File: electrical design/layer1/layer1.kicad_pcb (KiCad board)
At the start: 2 copper layers, 178 x 168.1 mm, 211 parts, among them J1 XT60-F, J2 1x07 2.54 FEMALE, J3 1x07 2.54 FEMALE, J4 XT30PW-F, J5 Conn_01x01_Socket, J6 Conn_01x01_Socket, J7 Conn_01x01_Socket, J8 Conn_01x01_Socket, Q1 MOSFET-NCH-FQP30N06L, Q2 MOSFET-NCH-AO3404A, SW1 SW_DPDT_x2, U1 CD74HC4067SM, U2 CD74HC4067SM

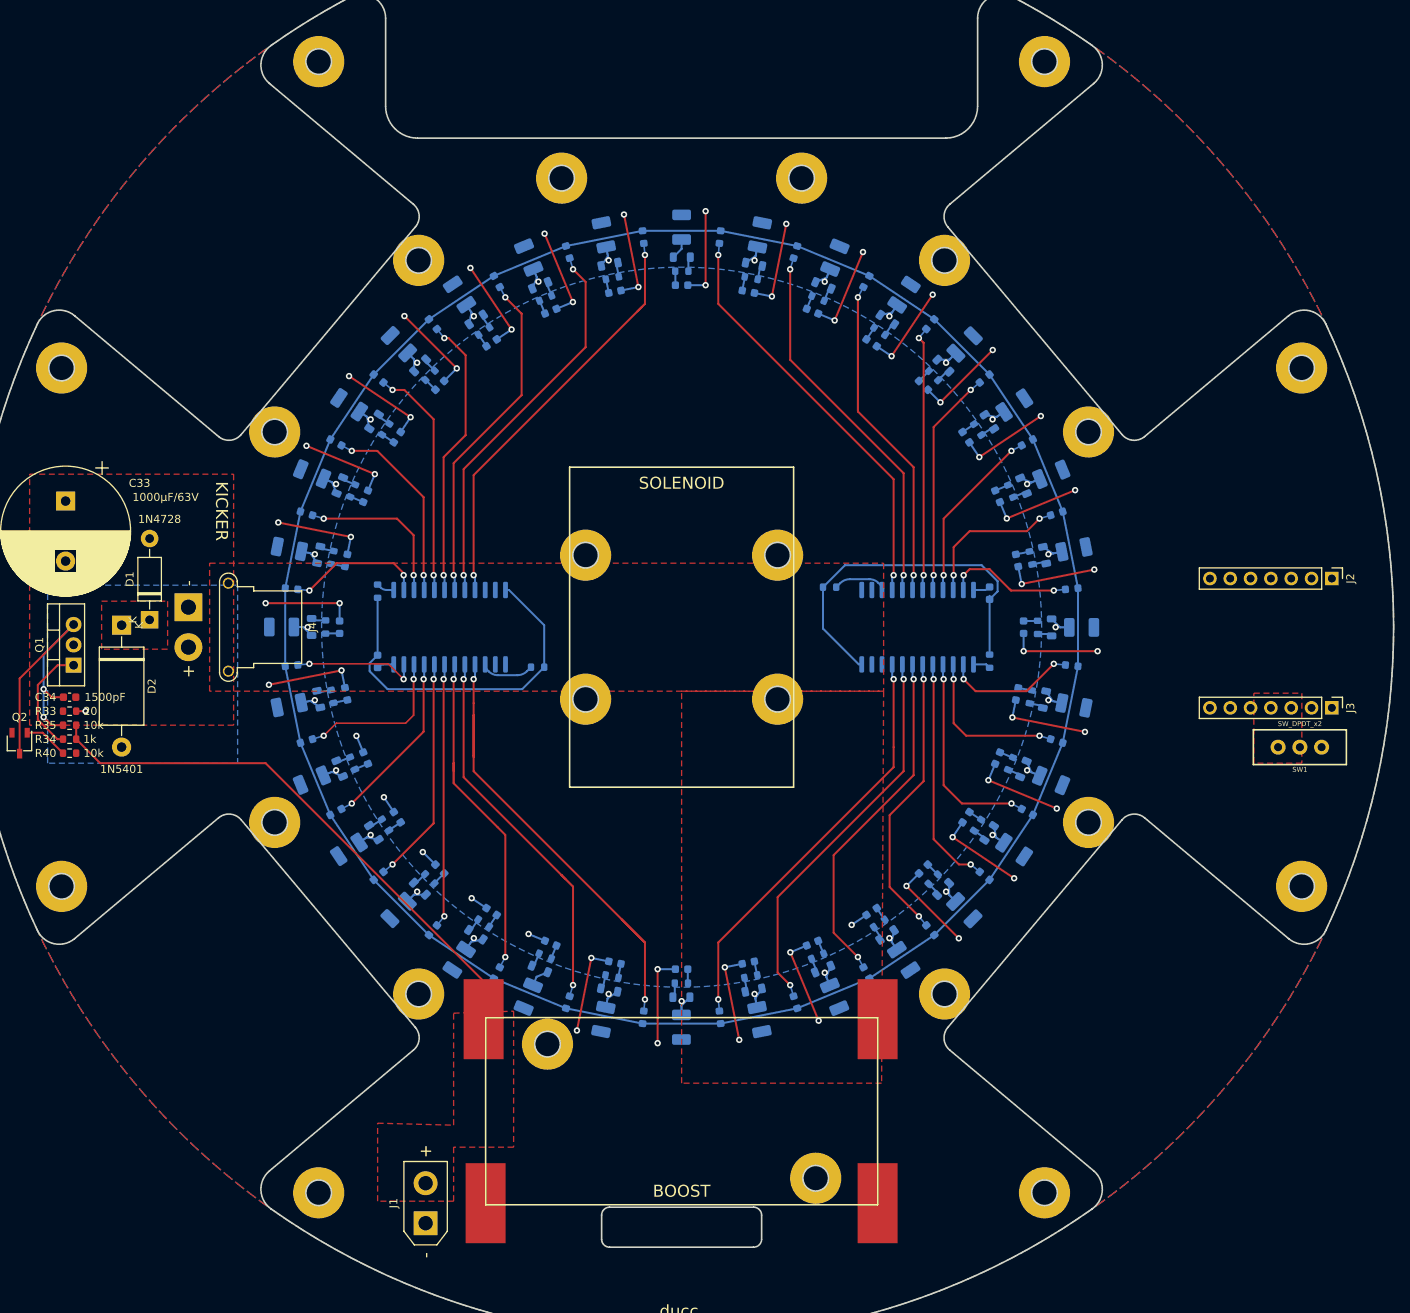
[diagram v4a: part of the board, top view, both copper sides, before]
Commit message: route l1 signal lines and resolve drc issues
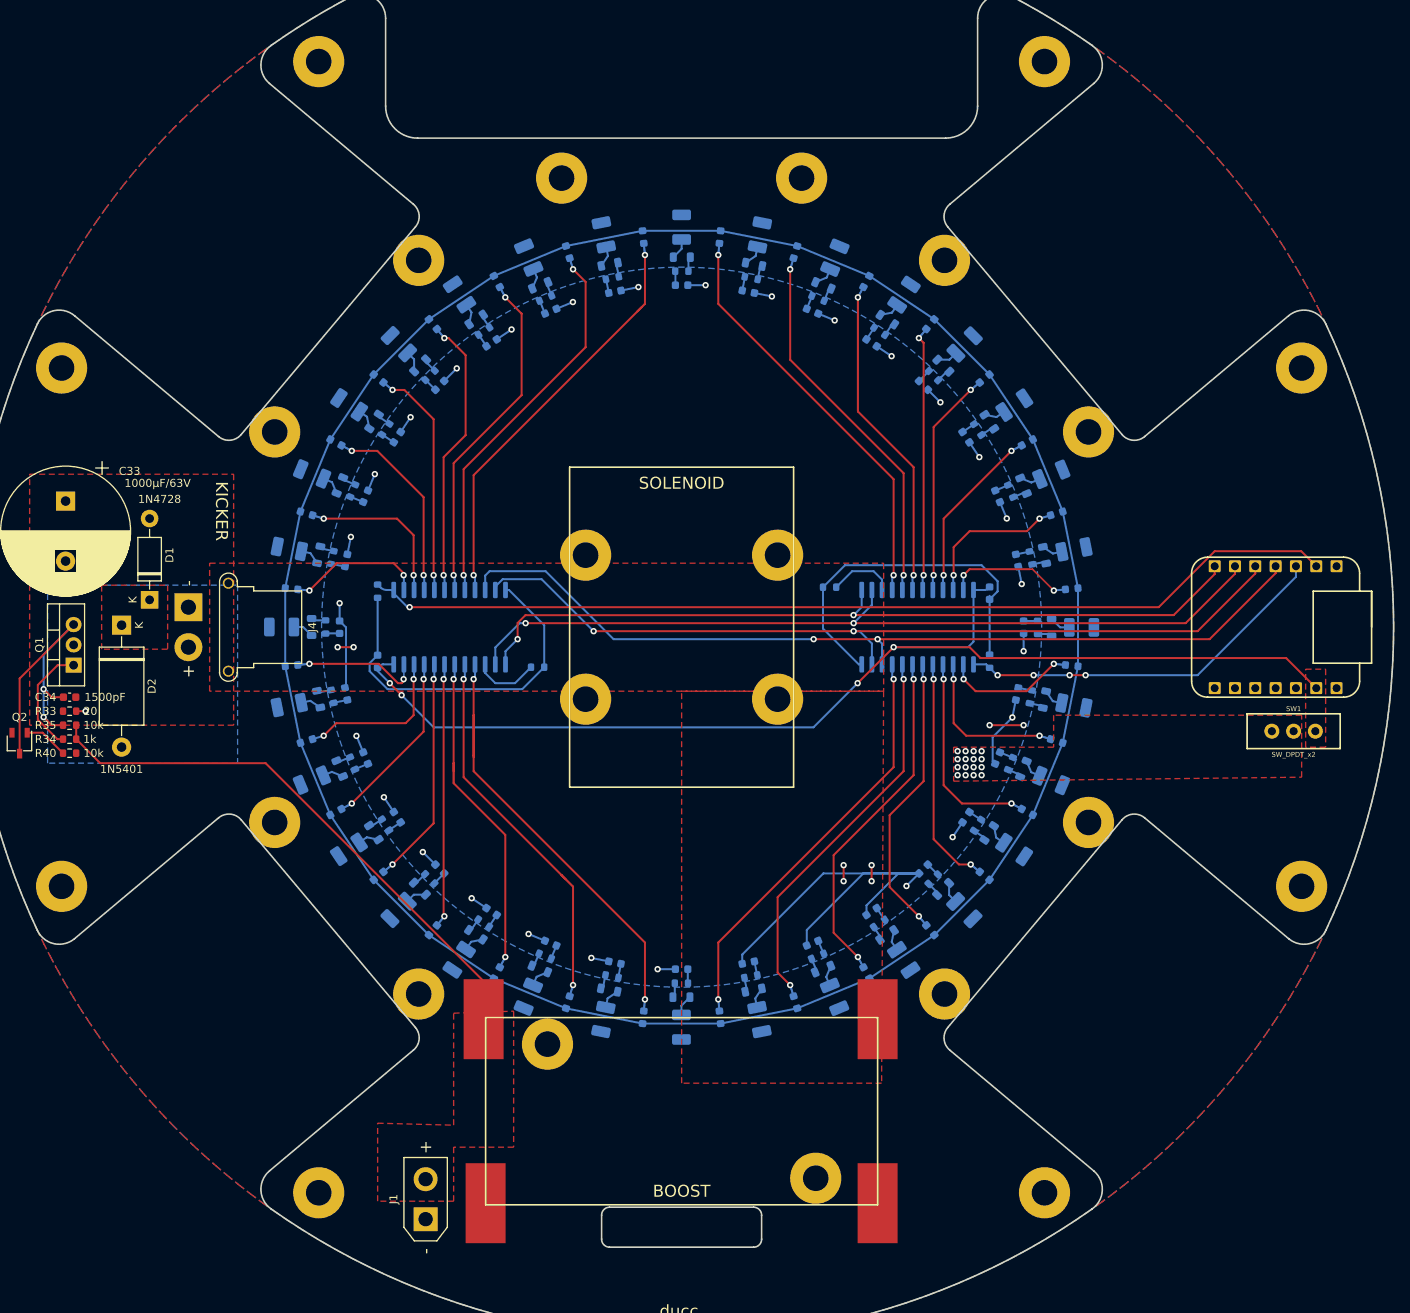
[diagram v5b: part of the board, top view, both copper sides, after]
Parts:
- removed J2, J3: 1x07 2.54 FEMALE, Connector_PinHeader_2.54mm:PinHeader_1x07_P2.54mm_Vertical
- added U3: MOUDLE-SEEEDUINO-XIAO-ESP32C3, libraries:xiao-esp32c3, F.Cu at (179.2, 105.0)
- moved D1 2.50 mm to (38.5, 101.6)
- moved SW1 2.15 mm to (181.5, 118.0), turned to -90 degrees
- moved J1 0.50 mm to (73.0, 179.0)
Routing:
- net GND: track 311.7 -> 131.6 mm, vias 58 -> 27
- net +3V3: track 4.59 -> 148.1 mm, vias 0 -> 4
- net /MUX1OUT: track 2.47 -> 122.6 mm, vias 0 -> 1
- net /S0: track 0.00 -> 112.0 mm, vias 0 -> 2
- net /S1: track 0.00 -> 107.9 mm, vias 0 -> 2
- net /S2: track 0.00 -> 104.4 mm, vias 0 -> 2
- net /S3: track 0.00 -> 100.0 mm, vias 0 -> 2
- net /MUX2OUT: track 2.19 -> 47.3 mm, vias 0 -> 4
- net Net-(SW1A-B): track 56.3 -> 66.6 mm, vias 0 -> 24
- net Net-(U1-I15): track 61.7 -> 59.0 mm
- net Net-(U1-I8): track 15.9 -> 17.9 mm
- net Net-(U2-~{E}): track 6.77 -> 8.29 mm
- net Net-(LED5-A): track 4.12 -> 2.65 mm, vias 1 -> 0
- net Net-(LED21-A): track 4.12 -> 2.65 mm, vias 1 -> 0
- net Net-(LED29-A): track 4.12 -> 2.65 mm, vias 1 -> 0
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- added copper zone on F.Cu, net Net-(SW1A-B)
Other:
- outline, holes or cut-outs redrawn

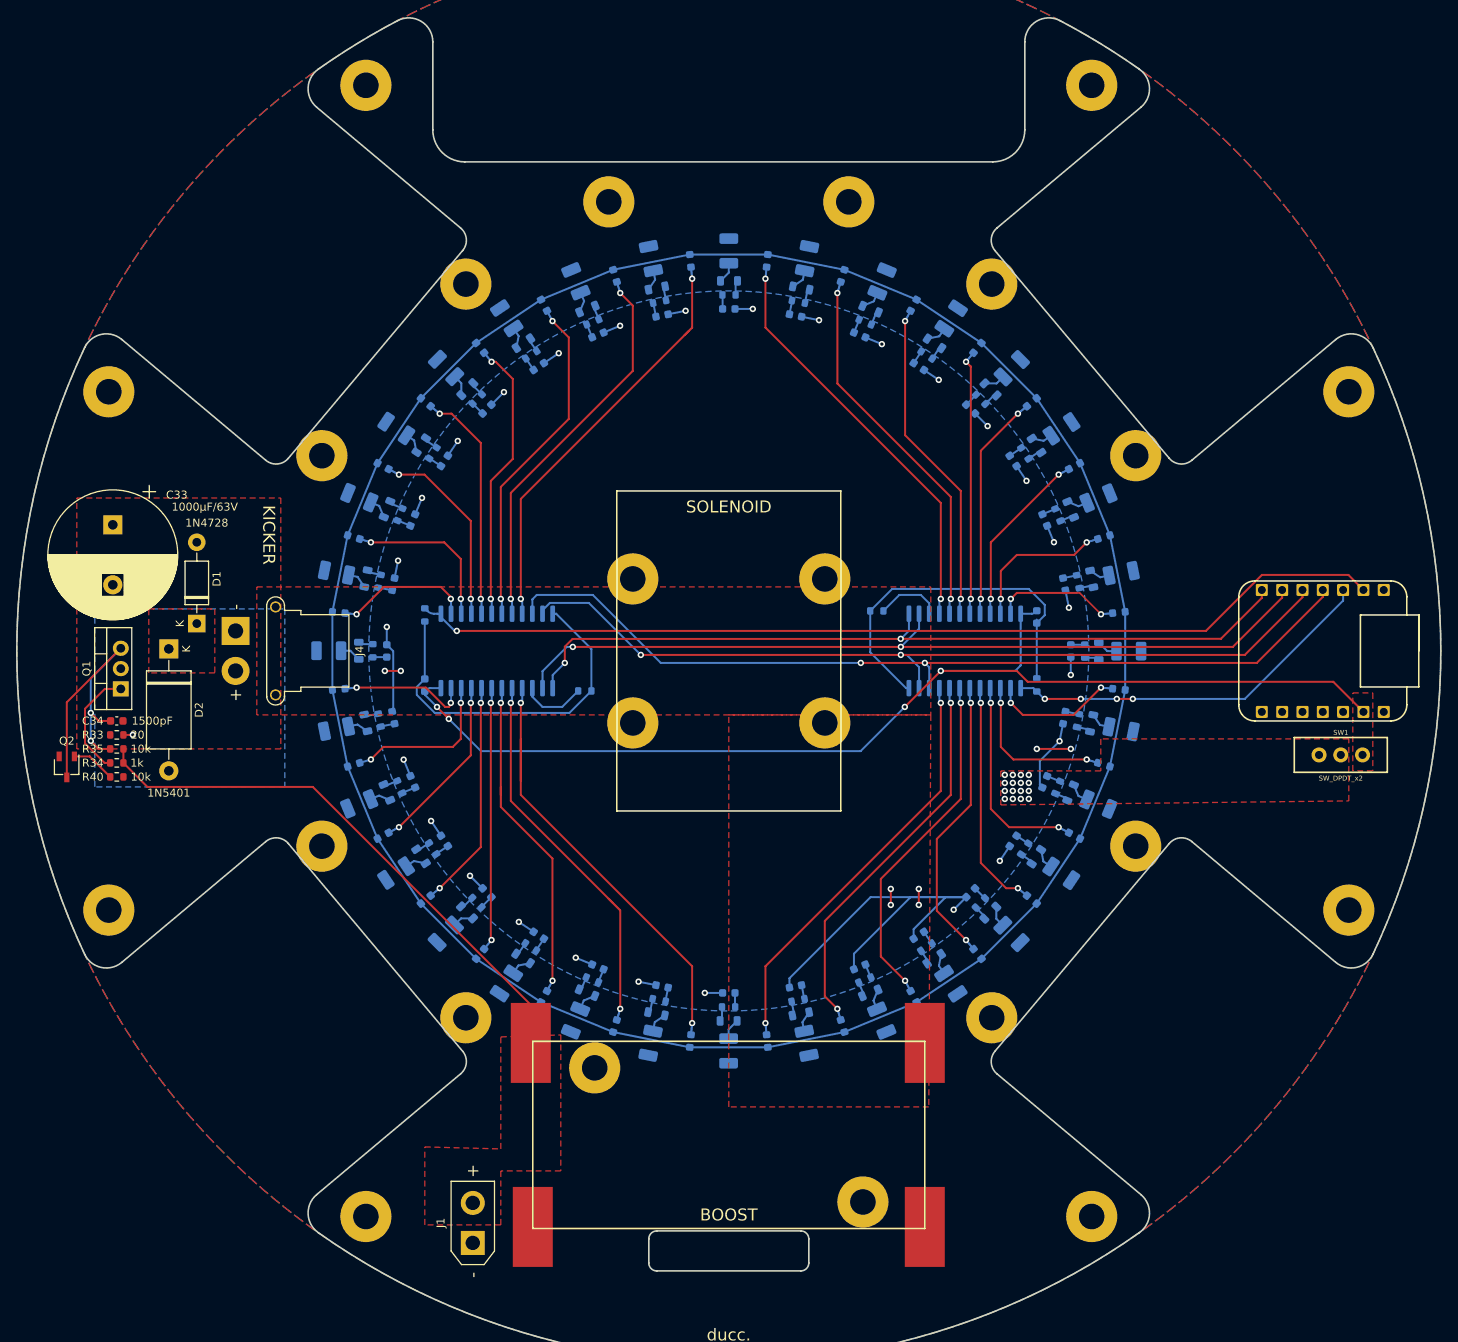
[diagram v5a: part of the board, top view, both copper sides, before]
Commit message: reposition kicker circuit and improve routing
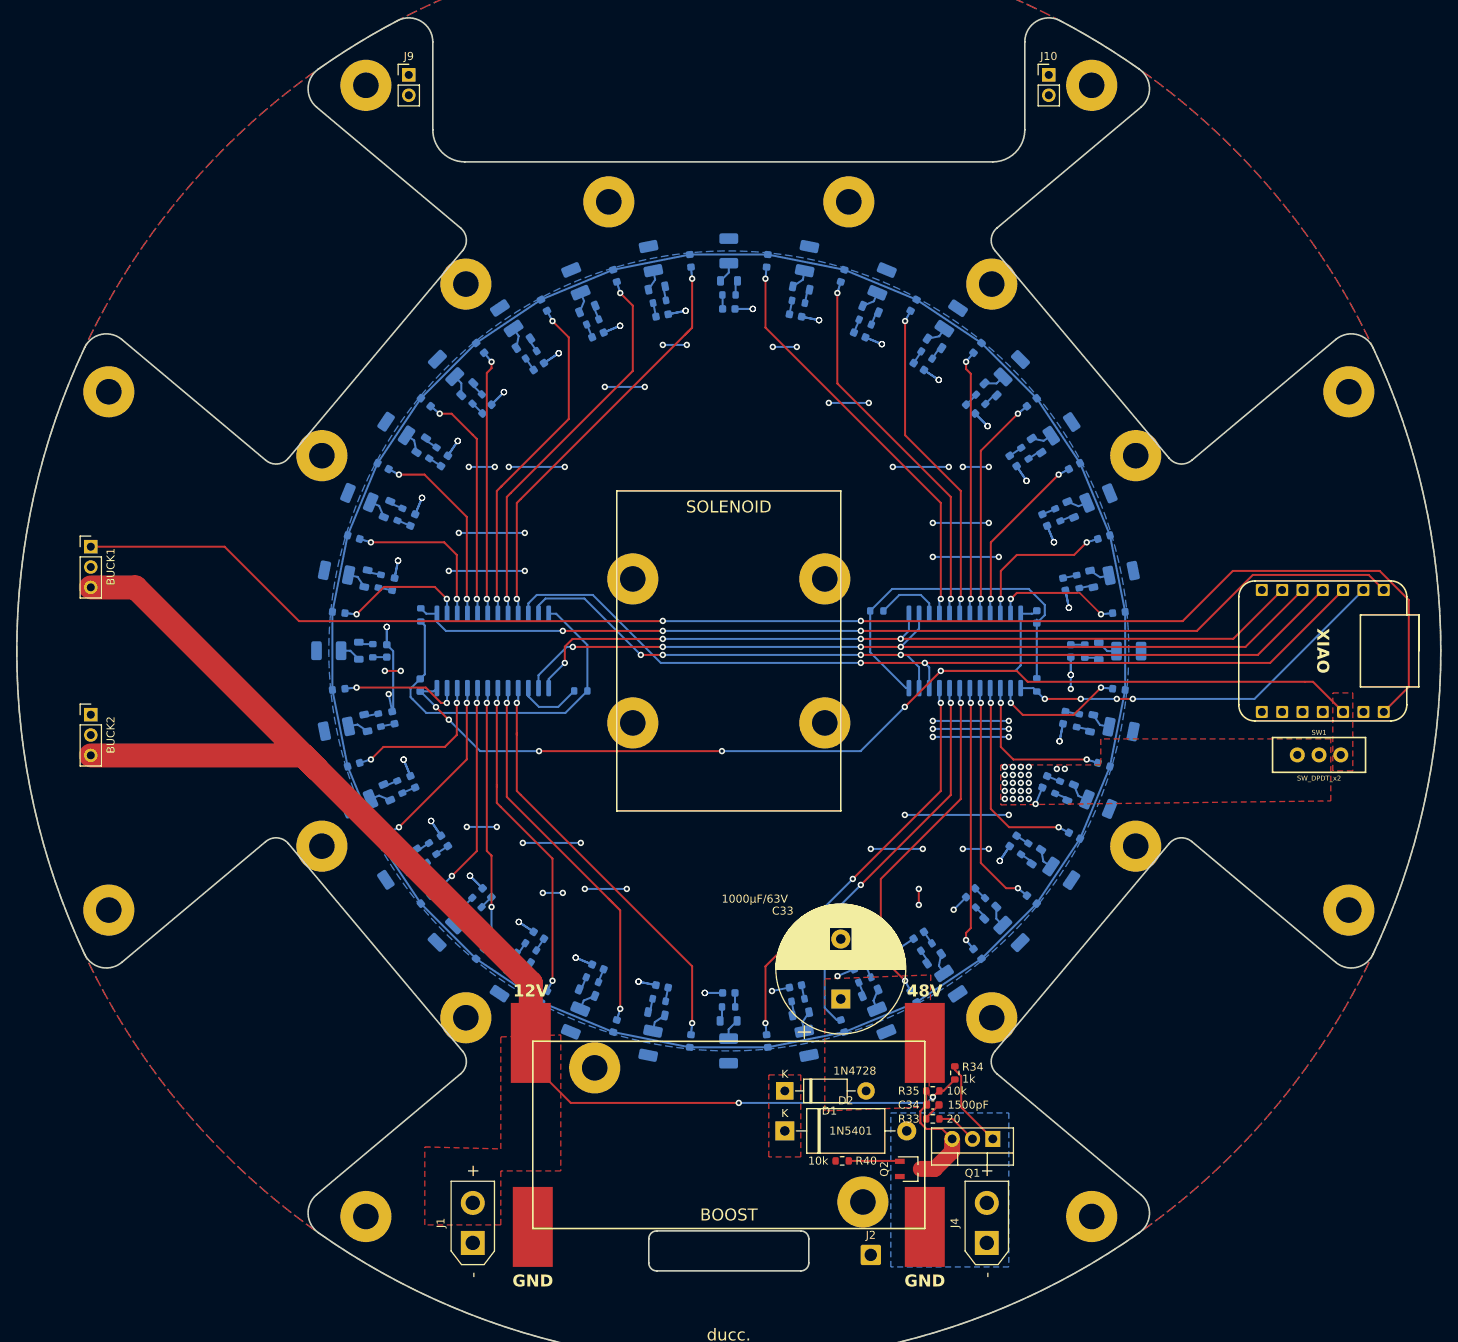
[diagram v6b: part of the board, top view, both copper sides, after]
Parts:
- added BUCK1: +5V, Connector_PinHeader_2.54mm:PinHeader_1x03_P2.54mm_Vertical, F.Cu at (25.2, 92.0)
- added BUCK2: +3V3, Connector_PinHeader_2.54mm:PinHeader_1x03_P2.54mm_Vertical, F.Cu at (25.2, 113.0)
- added J10: Conn_01x02_Pin, Connector_PinHeader_2.54mm:PinHeader_1x02_P2.54mm_Vertical, F.Cu at (145.0, 33.0)
- added J2: Conn_01x01_Socket, Connector_Wire:SolderWire-0.75sqmm_1x01_D1.25mm_OD2.3mm, F.Cu at (122.8, 180.5)
- added J9: Conn_01x02_Pin, Connector_PinHeader_2.54mm:PinHeader_1x02_P2.54mm_Vertical, F.Cu at (65.0, 33.0)
- J4: footprint Connector_AMASS:AMASS_XT30PW-F_1x02_P2.50mm_Horizontal -> Connector_AMASS:AMASS_XT30UPB-F_1x02_P5.0mm_Vertical
- moved Q1 122.7 mm to (138.0, 166.0), turned to 180 degrees
- moved J4 121.1 mm to (137.2, 179.0), turned to 90 degrees
- moved Q2 116.8 mm to (127.7, 169.8), turned to 0 degrees
- moved C34 112.7 mm to (130.5, 161.8)
- moved R33 112.7 mm to (130.5, 163.5)
- moved R34 111.7 mm to (133.2, 157.8), turned to 90 degrees
- moved R35 110.6 mm to (130.5, 160.0)
- moved C33 108.6 mm to (119.0, 148.5), turned to 90 degrees
- moved R40 102.6 mm to (119.2, 168.8), turned to 180 degrees
- moved D2 97.8 mm to (112.0, 165.0), turned to 0 degrees
- moved D1 93.9 mm to (112.0, 160.0), turned to 0 degrees
- moved SW1 2.72 mm to (178.8, 118.0)
- moved C35 0.58 mm to (66.4, 109.3)
- moved R36 0.50 mm to (66.5, 100.5)
- moved R37 0.50 mm to (86.5, 110.0)
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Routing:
- net +5V: track 0.00 -> 188.0 mm, vias 0 -> 2
- net GND: track 131.6 -> 280.6 mm, vias 27 -> 103
- net +12V: track 70.0 -> 170.7 mm, vias 0 -> 2
- net Net-(Q1-S): track 37.8 -> 16.2 mm, vias 2 -> 0
- net Net-(SW1A-B): track 66.6 -> 60.3 mm, vias 24 -> 26
- net Net-(U1-I15): track 59.0 -> 54.2 mm
- net Net-(D2-A): track 1.18 -> 5.17 mm, vias 1 -> 0
- net /S1: track 107.9 -> 111.2 mm, vias 2 -> 4
- net /MUX1OUT: track 122.6 -> 125.8 mm, vias 1 -> 3
- net Net-(U2-I3): track 37.7 -> 34.7 mm
- net Net-(Q1-G): track 14.0 -> 11.0 mm
- net Net-(C34-Pad1): track 0.00 -> 2.41 mm
- net Net-(U1-I13): track 44.7 -> 42.4 mm
- net /S0: track 112.0 -> 114.3 mm
- net /S2: track 104.4 -> 106.6 mm, vias 2 -> 4
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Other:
- board text added: "12V"
- board text added: "48V"
- board text added: "GND"
- board text added: "XIAO"
- board text removed: "KICKER"
